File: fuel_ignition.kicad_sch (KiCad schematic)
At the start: 51 parts, among them U12 VNL5050, U13 VNL5050, U14 VNL5050, U15 VNL5050, U16 IXDN602, U17 IXDN602

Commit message: Add additional IOs
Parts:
- JP6: footprint Connector_PinHeader_2.54mm:PinHeader_1x03_P2.54mm_Vertical -> Jumper:SolderJumper-3_P1.3mm_Open_RoundedPad1.0x1.5mm
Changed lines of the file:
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@@
 			)
 		)
-		(property "Footprint" "Connector_PinHeader_2.54mm:PinHeader_1x03_P2.54mm_Vertical"
+		(property "Footprint" "Jumper:SolderJumper-3_P1.3mm_Open_RoundedPad1.0x1.5mm"
 			(at 148.59 173.99 0)
 			(effects

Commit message: Pre MCU switch
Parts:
- removed D10, D12, D14: LED, LED_SMD:LED_0805_2012Metric, symbol Device:LED
- removed D11, D13, D15: D, Diode_SMD:D_SOD-323, symbol Device:D
- removed U12, U13, U14, U15: VNL5050, IC_Automotive:SOT-223-3_VNL5050, symbol IC_Automotive:VNL5050N3TR
- added D10, D12, D14: D, Diode_SMD:D_SOD-323, symbol Device:D
- added D11, D13, D15: LED, LED_SMD:LED_0805_2012Metric, symbol Device:LED
- added IC10, IC7, IC8, IC9: VNL5090N3-E, SOT230P700X180-4N, symbol IC_Automotive:VNL5090N3-E
- R58, R61, R64: value 2.4k -> 1k; Digikey Part Number 311-2.40KCRCT-ND -> 311-1.00KCRCT-ND; Manufacturer_Part_Number RC0805FR-072K4L -> RC0805FR-071KL; URL https://www.digikey.com/product-detail/en/yageo/RC0805FR-072K4L/311-2.40KCRCT-ND/730637 -> https://www.digikey.com/product-detail/en/yageo/RC0805FR-071KL/311-1.00KCRCT-ND/730391
- R59, R62, R65: value 1k -> 100k; Digikey Part Number 311-1.00KCRCT-ND -> 311-100KCRCT-ND; Manufacturer_Part_Number RC0805FR-071KL -> RC0805FR-07100KL; URL https://www.digikey.com/product-detail/en/yageo/RC0805FR-071KL/311-1.00KCRCT-ND/730391 -> https://www.digikey.com/product-detail/en/yageo/RC0805FR-07100KL/311-100KCRCT-ND/730491
- R60, R63, R66: value 100k -> 2.4k; Digikey Part Number 311-100KCRCT-ND -> 311-2.40KCRCT-ND; Manufacturer_Part_Number RC0805FR-07100KL -> RC0805FR-072K4L; URL https://www.digikey.com/product-detail/en/yageo/RC0805FR-07100KL/311-100KCRCT-ND/730491 -> https://www.digikey.com/product-detail/en/yageo/RC0805FR-072K4L/311-2.40KCRCT-ND/730637
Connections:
- net +12V: now also R55.1, R60.1, R63.1, R66.1; no longer JP6.3 (B), R55.2, R58.2, R61.2, R64.2
- net GND: now also R57.1, R59.1, R62.1, R65.1, IC10.3 (SOURCE), IC7.3 (SOURCE), IC8.3 (SOURCE), IC9.3 (SOURCE); no longer R57.2, R60.2, R63.2, R66.2
- net INJ-1-OUT: now also IC7.2 (DRAIN_1), IC7.4 (DRAIN_2)
- net INJ-1-TRIG: now also R57.2; no longer R57.1
- net INJ-2-OUT: now also D10.1 (K), IC8.2 (DRAIN_1), IC8.4 (DRAIN_2)
- net INJ-2-TRIG: now also R58.2; no longer R60.1
- net INJ-3-OUT: now also D12.1 (K), IC9.2 (DRAIN_1), IC9.4 (DRAIN_2)
- net INJ-3-TRIG: now also R61.2; no longer R63.1
- net INJ-4-OUT: now also D14.1 (K), IC10.2 (DRAIN_1), IC10.4 (DRAIN_2)
- net INJ-4-TRIG: now also R64.2; no longer R66.1
- net at R56.1: now also IC7.1 (INPUT)
- net at D8.2 (A): now also R55.2; no longer R55.1
- net at R58.1: now also IC8.1 (INPUT)
- net at R64.1: now also IC10.1 (INPUT)
- net at R61.1: now also IC9.1 (INPUT)
- new net: D13.2 (A), R63.2
- new net: D14.2 (A), D15.1 (K)
- new net: D11.2 (A), R60.2
- new net: D12.2 (A), D13.1 (K)
- new net: D15.2 (A), R66.2
- new net: D10.2 (A), D11.1 (K)
- new net RAW-BAT: JP6.3 (B)
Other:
- moved on the sheet: D8, D9, R55, R56, R57

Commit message: Fully connect all components
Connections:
- net RAW-BAT is gone; now on net VBAT: JP6.3 (B)
- net +12V renamed VBAT
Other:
- note added: "Ignition Voltage Selector"
- note removed: "?"
- note removed: "Divider or pulldown?"

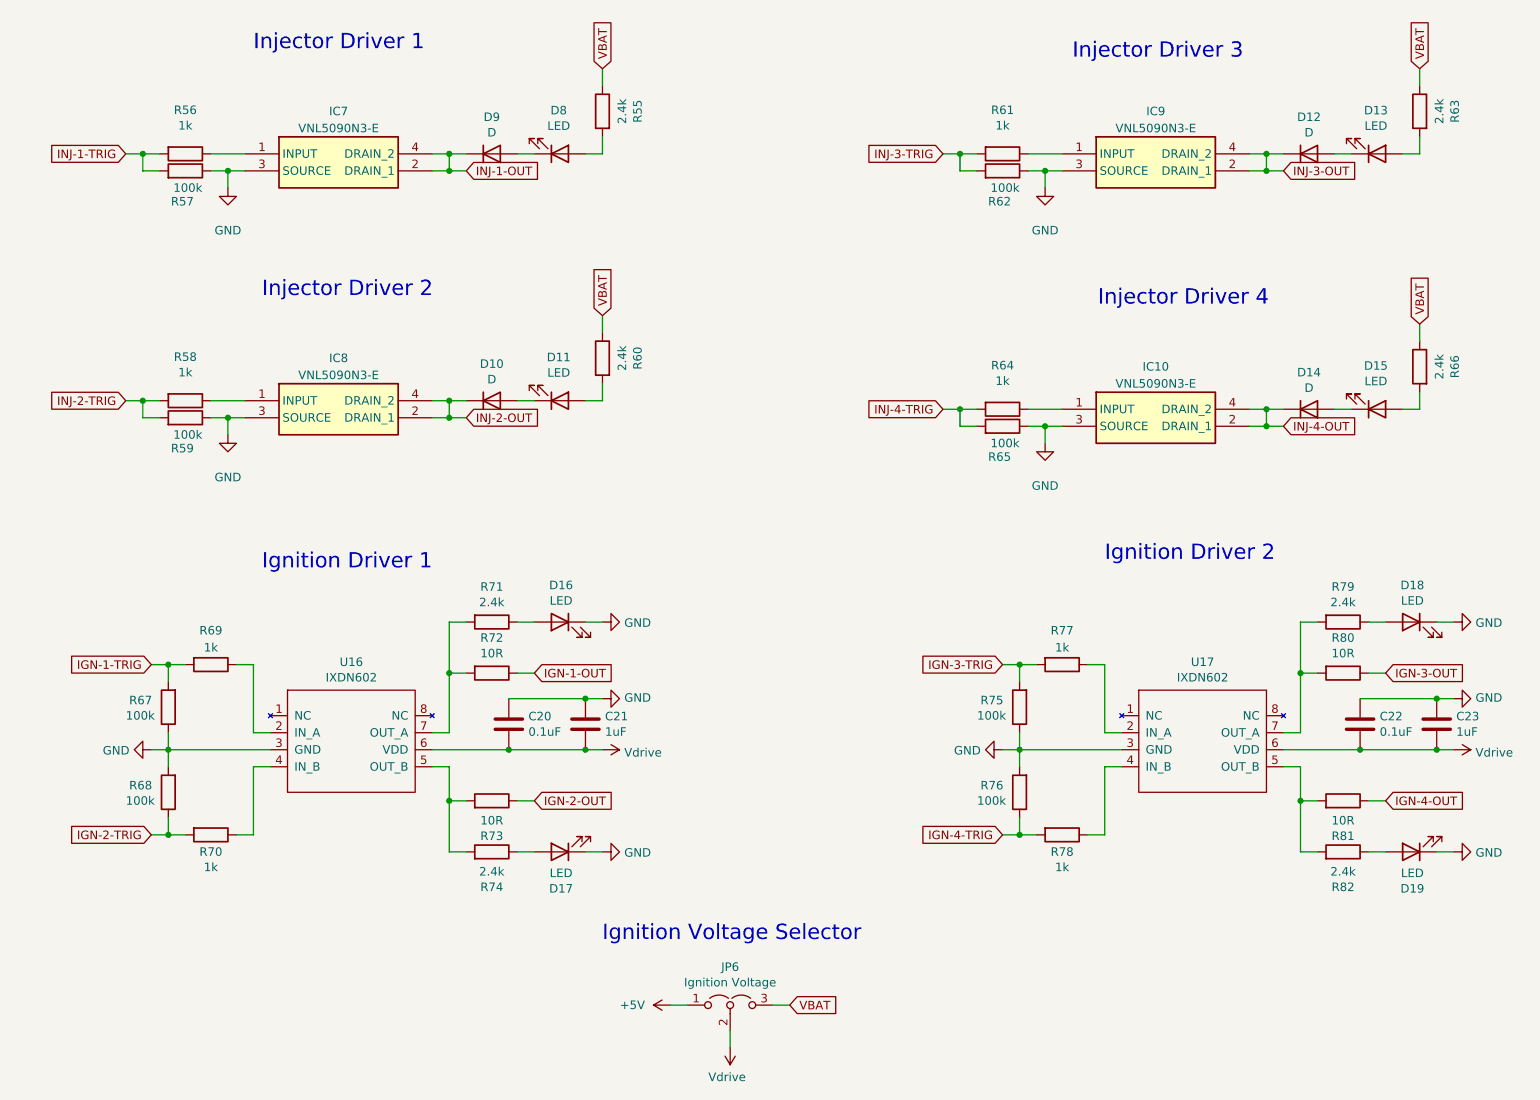
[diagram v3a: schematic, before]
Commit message: Updated reference layout
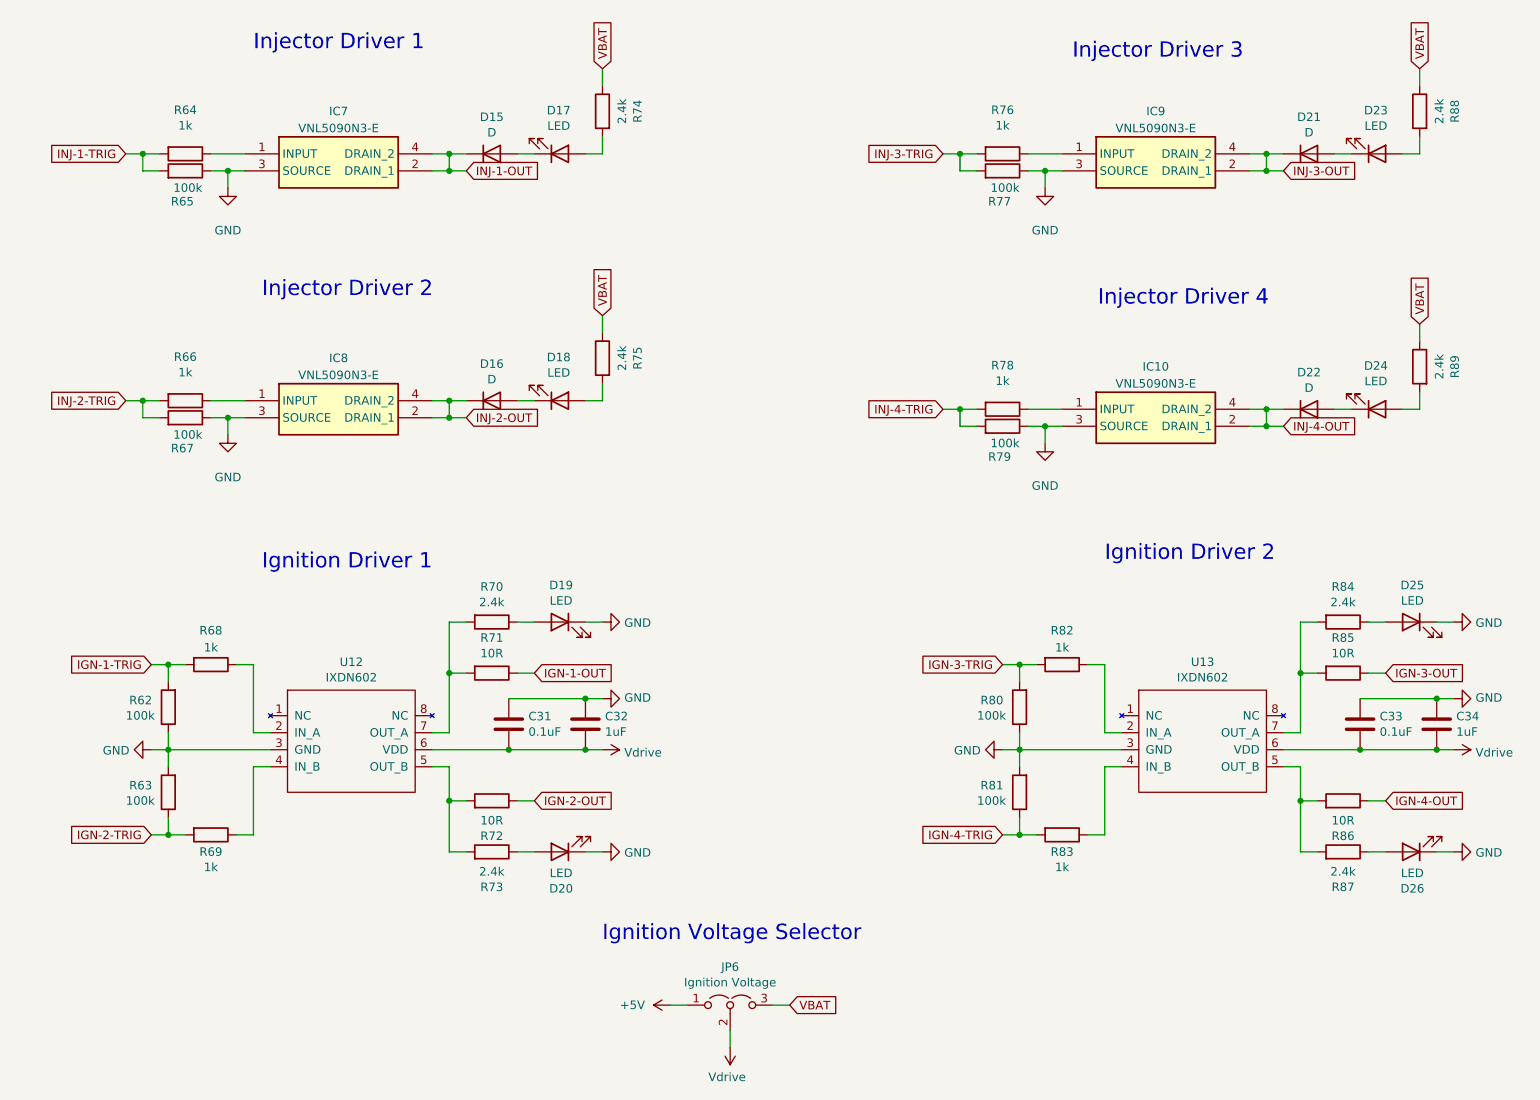
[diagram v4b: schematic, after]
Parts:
- renumbered C20 to C31, C21 to C32, C22 to C33, C23 to C34, D9 to D15, D10 to D16, D8 to D17, D11 to D18, D16 to D19, D17 to D20, D12 to D21, D14 to D22, D13 to D23, D15 to D24, D18 to D25, D19 to D26, R67 to R62, R68 to R63, R56 to R64, R57 to R65, R58 to R66, R59 to R67, R69 to R68, R70 to R69, R71 to R70, R72 to R71, R73 to R72, R74 to R73, R55 to R74, R60 to R75, R61 to R76, R62 to R77, R64 to R78, R65 to R79, R75 to R80, R76 to R81, R77 to R82, R78 to R83, R79 to R84, R80 to R85, R81 to R86, R82 to R87, R63 to R88, R66 to R89, U16 to U12, U17 to U13

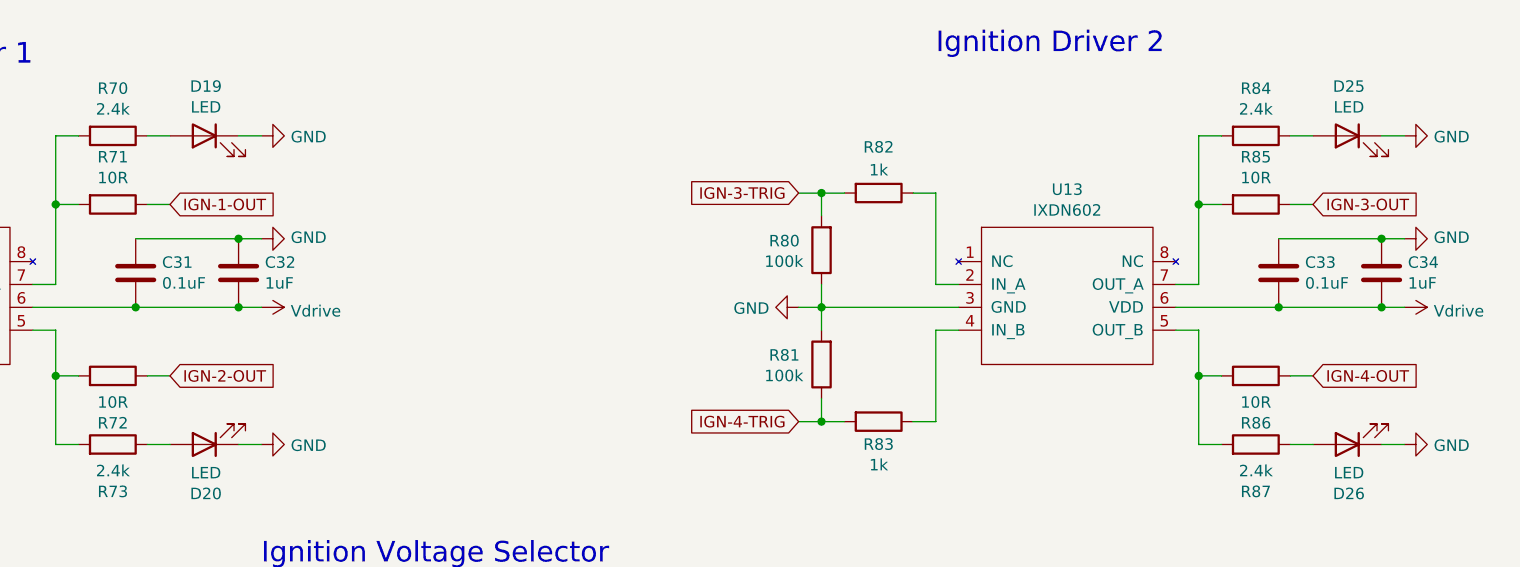
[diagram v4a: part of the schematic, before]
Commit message: Change power layout, add low frequency crystal
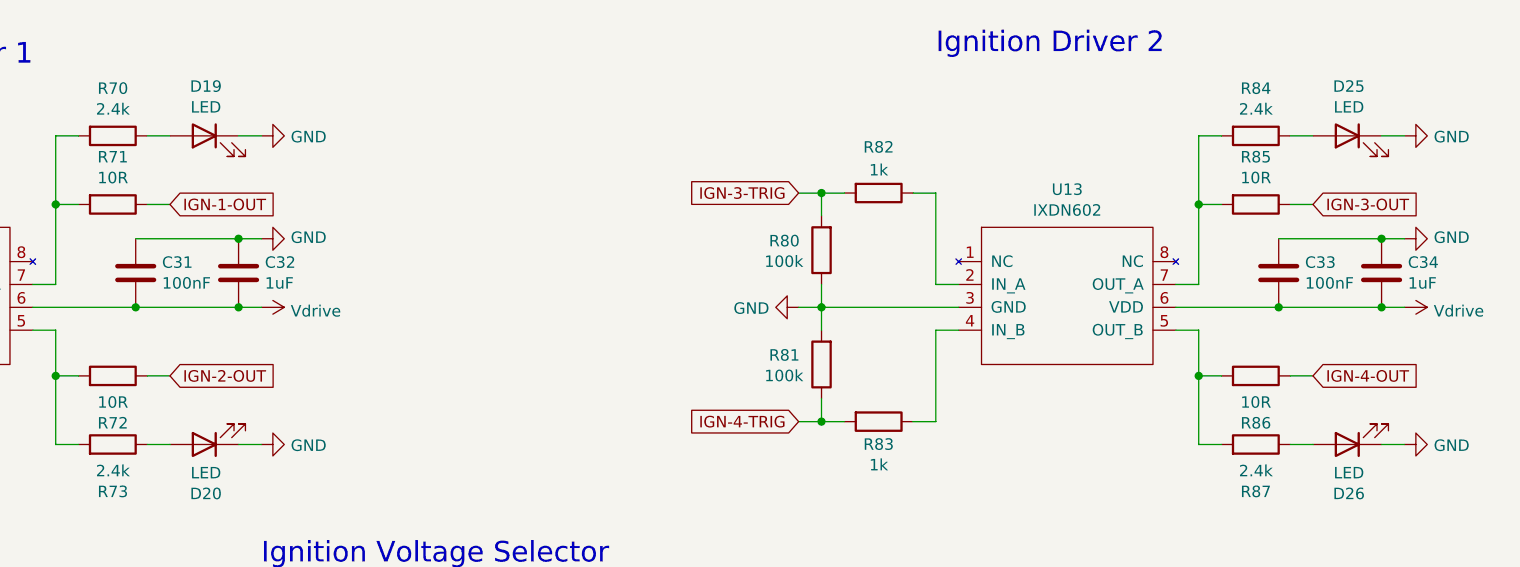
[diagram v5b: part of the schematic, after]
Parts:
- C31, C33: value 0.1uF -> 100nF
